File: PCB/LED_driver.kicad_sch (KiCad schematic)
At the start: 20 parts, among them J3 LED_GRBWA, J4 LED 5050, Q3 UMW30N06, Q4 UMW30N06, Q5 UMW30N06, U7 MCP1416, U8 MCP1416

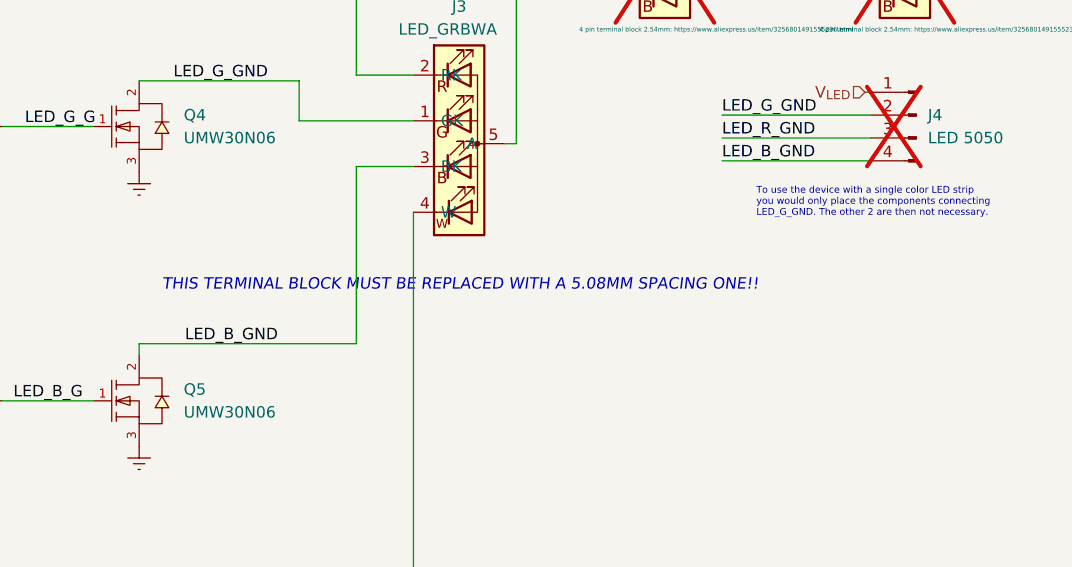
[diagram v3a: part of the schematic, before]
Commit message: design v1.0 - complete redesign
* redid schematic
* changed to screw terminal
* added W channel for RGBW strips
* did layout
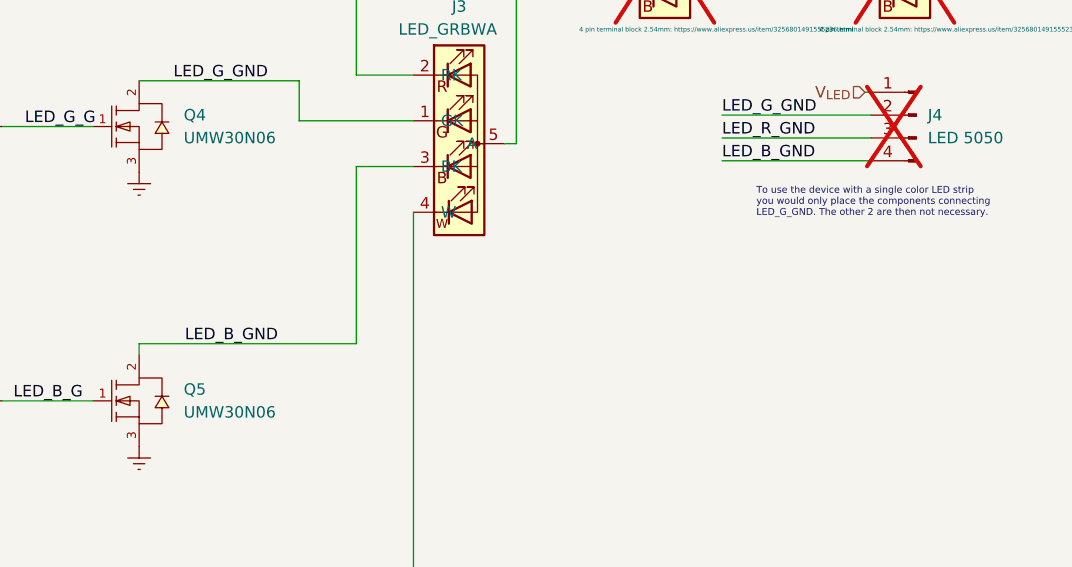
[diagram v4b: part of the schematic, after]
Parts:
- D2, J4: LCSC (none) -> -
- J3: LCSC (none) -> C5188445; Note (none) -> 5 pin 2.54 Pitch Terminal Block
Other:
- note removed: "THIS TERMINAL BLOCK MUST BE REPLACED WITH A 5.08MM SPACING ONE!!"
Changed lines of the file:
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@@
     (effects (font (size 1.27 1.27)) (justify left bottom))
-  )
-  (text "THIS TERMINAL BLOCK MUST BE REPLACED WITH A 5.08MM SPACING ONE!!"
-    (at 161.29 96.52 0)
-    (effects (font (size 1.27 1.27) italic) (justify left bottom))
   )
   (label "LED_R_GND" (at 223.52 79.375 0) (fields_autoplaced)
@@
         )
       )
-      (project "dumb-led-driver"
+      (project "iot_pwm_leddriver"
         (path "/b6358773-9a18-4eb2-bc1b-d38393a8df39/906d9b01-c5b2-4615-86e8-3c8294737d59"
           (reference "C4") (unit 1)
@@
         )
       )
-      (project "dumb-led-driver"
+      (project "iot_pwm_leddriver"
         (path "/b6358773-9a18-4eb2-bc1b-d38393a8df39/906d9b01-c5b2-4615-86e8-3c8294737d59"
           (reference "C3") (unit 1)
@@
         )
       )
-      (project "dumb-led-driver"
+      (project "iot_pwm_leddriver"
         (path "/b6358773-9a18-4eb2-bc1b-d38393a8df39/906d9b01-c5b2-4615-86e8-3c8294737d59"
           (reference "#PWR015") (unit 1)
@@
         )
       )
-      (project "dumb-led-driver"
+      (project "iot_pwm_leddriver"
         (path "/b6358773-9a18-4eb2-bc1b-d38393a8df39/906d9b01-c5b2-4615-86e8-3c8294737d59"
           (reference "#PWR016") (unit 1)
@@
         )
       )
-      (project "dumb-led-driver"
+      (project "iot_pwm_leddriver"
         (path "/b6358773-9a18-4eb2-bc1b-d38393a8df39/906d9b01-c5b2-4615-86e8-3c8294737d59"
           (reference "R10") (unit 1)
@@
       (effects (font (size 1.27 1.27)) hide)
     )
+    (property "LCSC" "-" (at 245.11 76.835 0)
+      (effects (font (size 1.27 1.27)) hide)
+    )
     (pin "1")
     (pin "2")
@@
         )
       )
-      (project "dumb-led-driver"
+      (project "iot_pwm_leddriver"
         (path "/b6358773-9a18-4eb2-bc1b-d38393a8df39/906d9b01-c5b2-4615-86e8-3c8294737d59"
           (reference "J4") (unit 1)
@@
         )
       )
-      (project "dumb-led-driver"
+      (project "iot_pwm_leddriver"
         (path "/b6358773-9a18-4eb2-bc1b-d38393a8df39/906d9b01-c5b2-4615-86e8-3c8294737d59"
           (reference "#PWR013") (unit 1)
@@
       (effects (font (size 1.27 1.27)) hide)
     )
+    (property "LCSC" "-" (at 217.17 58.42 0)
+      (effects (font (size 1.27 1.27)) hide)
+    )
     (pin "1")
     (pin "2")
@@
         )
       )
-      (project "dumb-led-driver"
+      (project "iot_pwm_leddriver"
         (path "/b6358773-9a18-4eb2-bc1b-d38393a8df39/906d9b01-c5b2-4615-86e8-3c8294737d59"
           (reference "D4") (unit 1)
@@
         )
       )
-      (project "dumb-led-driver"
+      (project "iot_pwm_leddriver"
         (path "/b6358773-9a18-4eb2-bc1b-d38393a8df39/906d9b01-c5b2-4615-86e8-3c8294737d59"
           (reference "R8") (unit 1)
@@
     )
     (property "LCSC" "C83775 " (at 113.665 44.45 0)
+      (effects (font (size 1.27 1.27)) hide)
+    )
+    (property "Description" "alternatively: https://www.lcsc.com/product-detail/Gate-Drive-ICs_JSMSEMI-MCP1416T-E-OT-JSM_C18195002.html" (at 113.665 44.45 0)
       (effects (font (size 1.27 1.27)) hide)
     )
@@
         )
       )
-      (project "dumb-led-driver"
+      (project "iot_pwm_leddriver"
         (path "/b6358773-9a18-4eb2-bc1b-d38393a8df39/906d9b01-c5b2-4615-86e8-3c8294737d59"
           (reference "U2") (unit 1)
@@
         )
       )
-      (project "dumb-led-driver"
+      (project "iot_pwm_leddriver"
         (path "/b6358773-9a18-4eb2-bc1b-d38393a8df39/906d9b01-c5b2-4615-86e8-3c8294737d59"
           (reference "C2") (unit 1)
@@
         )
       )
-      (project "dumb-led-driver"
+      (project "iot_pwm_leddriver"
         (path "/b6358773-9a18-4eb2-bc1b-d38393a8df39/906d9b01-c5b2-4615-86e8-3c8294737d59"
           (reference "#PWR026") (unit 1)
@@
         )
       )
-      (project "dumb-led-driver"
+      (project "iot_pwm_leddriver"
         (path "/b6358773-9a18-4eb2-bc1b-d38393a8df39/906d9b01-c5b2-4615-86e8-3c8294737d59"
           (reference "Q4") (unit 1)
@@
         )
       )
-      (project "dumb-led-driver"
+      (project "iot_pwm_leddriver"
         (path "/b6358773-9a18-4eb2-bc1b-d38393a8df39/906d9b01-c5b2-4615-86e8-3c8294737d59"
           (reference "R7") (unit 1)
@@
         )
       )
-      (project "dumb-led-driver"
+      (project "iot_pwm_leddriver"
         (path "/b6358773-9a18-4eb2-bc1b-d38393a8df39/906d9b01-c5b2-4615-86e8-3c8294737d59"
           (reference "R11") (unit 1)
@@
       (effects (font (size 1.27 1.27)) hide)
     )
+    (property "LCSC" "-" (at 243.84 58.42 0)
+      (effects (font (size 1.27 1.27)) hide)
+    )
     (pin "1")
     (pin "2")
@@
         )
       )
-      (project "dumb-led-driver"
+      (project "iot_pwm_leddriver"
         (path "/b6358773-9a18-4eb2-bc1b-d38393a8df39/906d9b01-c5b2-4615-86e8-3c8294737d59"
           (reference "D3") (unit 1)
@@
     )
     (property "LCSC" "C83775 " (at 115.57 140.97 0)
+      (effects (font (size 1.27 1.27)) hide)
+    )
+    (property "Description" "alternatively: https://www.lcsc.com/product-detail/Gate-Drive-ICs_JSMSEMI-MCP1416T-E-OT-JSM_C18195002.html" (at 115.57 140.97 0)
       (effects (font (size 1.27 1.27)) hide)
     )
@@
         )
       )
-      (project "dumb-led-driver"
+      (project "iot_pwm_leddriver"
         (path "/b6358773-9a18-4eb2-bc1b-d38393a8df39/906d9b01-c5b2-4615-86e8-3c8294737d59"
           (reference "U3") (unit 1)
@@
     )
     (property "LCSC" "C83775 " (at 114.935 108.585 0)
+      (effects (font (size 1.27 1.27)) hide)
+    )
+    (property "Description" "alternatively: https://www.lcsc.com/product-detail/Gate-Drive-ICs_JSMSEMI-MCP1416T-E-OT-JSM_C18195002.html" (at 114.935 108.585 0)
       (effects (font (size 1.27 1.27)) hide)
     )
@@
         )
       )
-      (project "dumb-led-driver"
+      (project "iot_pwm_leddriver"
         (path "/b6358773-9a18-4eb2-bc1b-d38393a8df39/906d9b01-c5b2-4615-86e8-3c8294737d59"
           (reference "U5") (unit 1)
@@
         )
       )
-      (project "dumb-led-driver"
+      (project "iot_pwm_leddriver"
         (path "/b6358773-9a18-4eb2-bc1b-d38393a8df39/906d9b01-c5b2-4615-86e8-3c8294737d59"
           (reference "#PWR020") (unit 1)
@@
         )
       )
-      (project "dumb-led-driver"
+      (project "iot_pwm_leddriver"
         (path "/b6358773-9a18-4eb2-bc1b-d38393a8df39/906d9b01-c5b2-4615-86e8-3c8294737d59"
           (reference "Q1") (unit 1)
@@
         )
       )
-      (project "dumb-led-driver"
+      (project "iot_pwm_leddriver"
         (path "/b6358773-9a18-4eb2-bc1b-d38393a8df39/906d9b01-c5b2-4615-86e8-3c8294737d59"
           (reference "#PWR012") (unit 1)
@@
     )
     (property "LCSC" "C83775 " (at 113.665 78.105 0)
+      (effects (font (size 1.27 1.27)) hide)
+    )
+    (property "Description" "alternatively: https://www.lcsc.com/product-detail/Gate-Drive-ICs_JSMSEMI-MCP1416T-E-OT-JSM_C18195002.html" (at 113.665 78.105 0)
       (effects (font (size 1.27 1.27)) hide)
     )
@@
         )
       )
-      (project "dumb-led-driver"
+      (project "iot_pwm_leddriver"
         (path "/b6358773-9a18-4eb2-bc1b-d38393a8df39/906d9b01-c5b2-4615-86e8-3c8294737d59"
           (reference "U4") (unit 1)
@@
         )
       )
-      (project "dumb-led-driver"
+      (project "iot_pwm_leddriver"
         (path "/b6358773-9a18-4eb2-bc1b-d38393a8df39/906d9b01-c5b2-4615-86e8-3c8294737d59"
           (reference "Q2") (unit 1)
@@
         )
       )
-      (project "dumb-led-driver"
+      (project "iot_pwm_leddriver"
         (path "/b6358773-9a18-4eb2-bc1b-d38393a8df39/906d9b01-c5b2-4615-86e8-3c8294737d59"
           (reference "#PWR027") (unit 1)
@@
         )
       )
-      (project "dumb-led-driver"
+      (project "iot_pwm_leddriver"
         (path "/b6358773-9a18-4eb2-bc1b-d38393a8df39/906d9b01-c5b2-4615-86e8-3c8294737d59"
           (reference "#PWR024") (unit 1)
@@
         )
       )
-      (project "dumb-led-driver"
+      (project "iot_pwm_leddriver"
         (path "/b6358773-9a18-4eb2-bc1b-d38393a8df39/906d9b01-c5b2-4615-86e8-3c8294737d59"
           (reference "Q3") (unit 1)
@@
       (effects (font (size 1.27 1.27)) hide)
     )
-    (property "Datasheet" "" (at 191.77 90.17 0)
-      (effects (font (size 1.27 1.27)) hide)
-    )
-    (property "Description" "FIX SELECTION OF TERMINAL BLOCK, MUST SOURCE ONE CORRECTLY!!!" (at 191.77 90.17 0)
+    (property "Datasheet" "https://www.lcsc.com/product-detail/Screw-terminal_MAX-MX128-2-54-05P-GN01-Cu-Y-A_C5188445.html" (at 191.77 90.17 0)
+      (effects (font (size 1.27 1.27)) hide)
+    )
+    (property "Description" "MX128-2.54-05P-GN01-Cu-Y-A" (at 191.77 90.17 0)
+      (effects (font (size 1.27 1.27)) hide)
+    )
+    (property "LCSC" "C5188445" (at 191.77 90.17 0)
+      (effects (font (size 1.27 1.27)) hide)
+    )
+    (property "Note" "5 pin 2.54 Pitch Terminal Block" (at 191.77 90.17 0)
       (effects (font (size 1.27 1.27)) hide)
     )
@@
     (pin "5")
     (instances
-      (project "dumb-led-driver"
+      (project "iot_pwm_leddriver"
         (path "/b6358773-9a18-4eb2-bc1b-d38393a8df39/906d9b01-c5b2-4615-86e8-3c8294737d59"
           (reference "J3") (unit 1)
@@
         )
       )
-      (project "dumb-led-driver"
+      (project "iot_pwm_leddriver"
         (path "/b6358773-9a18-4eb2-bc1b-d38393a8df39/906d9b01-c5b2-4615-86e8-3c8294737d59"
           (reference "C6") (unit 1)

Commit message: schematic and layout cleanup
* plus BOM finalization
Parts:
- removed D2: LED_RBGA, TerminalBlock_Phoenix:TerminalBlock_Phoenix_MPT-0,5-4-2.54_1x04_P2.54mm_Horizontal, symbol Device:LED_RBGA
- removed J4: LED 5050, Connector_PinHeader_2.54mm:PinHeader_1x04_P2.54mm_Vertical, symbol Connector:Conn_01x04_Male
- D2: Note 4 pin terminal block 2.54mm: https://www.aliexpress.us/item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 -> solder wire connector
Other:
- note added: "5m 5050 RGB LED Strip expected to draw max ~6A Math: P = VI, I_{total} = (Num_{LEDs}/m) * length(m) (.24W * 60 LEDs/m * 5m)/12V = 6A (But, will be lower irl due to R of copper in LED strip) Fuse rating = (Current / .75) = (6/.75) = 8A"
- note added: "This component is a stand-in for the LED strip, and corresponds to the screw terminal block on the board"
- note removed: "5m 5050 LED Strip expected to draw max ~6A Math: P = VI, I_{total} = (Num_{LEDs}/m) * length(m) (.24W * 60 LEDs/m * 5m)/12V = 6A (But, will be lower irl due to R of copper in LED strip) Fuse rating = (Current / .75) = (6/.75) = 8A"
- note removed: "This component is a stand-in for the LED strip, and corresponds to the strain relief connector on the board"
- note removed: "To use the device with a single color LED strip you would only place the components connecting LED_G_GND. The other 2 are then not necessary."
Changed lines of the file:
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@@
   (junction (at 113.665 66.675) (diameter 0) (color 0 0 0 0)
   )
-  (junction (at 238.76 58.42) (diameter 0) (color 0 0 0 0)
-  )
   (junction (at 212.09 53.34) (diameter 0) (color 0 0 0 0)
   )
   (junction (at 114.935 116.205) (diameter 0) (color 0 0 0 0)
   )
-  (junction (at 238.76 53.34) (diameter 0) (color 0 0 0 0)
-  )
   (junction (at 113.665 52.07) (diameter 0) (color 0 0 0 0)
   )
@@
     (stroke (width 0) (type default))
   )
-  (wire (pts (xy 238.76 58.42) (xy 238.76 63.5))
-    (stroke (width 0) (type default))
-  )
-  (wire (pts (xy 223.52 79.375) (xy 240.03 79.375))
-    (stroke (width 0) (type default))
-  )
   (wire (pts (xy 114.935 98.425) (xy 127.635 98.425))
     (stroke (width 0) (type default))
@@
     (stroke (width 0) (type default))
   )
-  (wire (pts (xy 238.76 46.99) (xy 238.76 53.34))
-    (stroke (width 0) (type default))
-  )
   (wire (pts (xy 159.385 134.62) (xy 189.23 134.62))
     (stroke (width 0) (type default))
   )
-  (wire (pts (xy 239.395 74.295) (xy 240.03 74.295))
-    (stroke (width 0) (type default))
-  )
   (wire (pts (xy 126.365 34.29) (xy 126.365 33.02))
     (stroke (width 0) (type default))
   )
-  (wire (pts (xy 223.52 81.915) (xy 240.03 81.915))
-    (stroke (width 0) (type default))
-  )
   (wire (pts (xy 212.09 48.26) (xy 212.09 53.34))
     (stroke (width 0) (type default))
   )
-  (wire (pts (xy 223.52 76.835) (xy 240.03 76.835))
-    (stroke (width 0) (type default))
-  )
   (wire (pts (xy 126.365 52.07) (xy 113.665 52.07))
     (stroke (width 0) (type default))
@@
     (stroke (width 0) (type default))
   )
-  (wire (pts (xy 248.92 46.99) (xy 238.76 46.99))
-    (stroke (width 0) (type default))
-  )
   (wire (pts (xy 128.27 130.81) (xy 128.27 132.08))
     (stroke (width 0) (type default))
@@
     (stroke (width 0) (type default))
   )
-  (wire (pts (xy 238.76 53.34) (xy 238.76 58.42))
-    (stroke (width 0) (type default))
-  )
   (wire (pts (xy 127.635 98.425) (xy 127.635 99.695))
     (stroke (width 0) (type default))
@@
     (stroke (width 0) (type default))
   )
-  (wire (pts (xy 248.92 58.42) (xy 248.92 46.99))
-    (stroke (width 0) (type default))
-  )
   (wire (pts (xy 212.09 53.34) (xy 212.09 58.42))
     (stroke (width 0) (type default))
@@
     (stroke (width 0) (type default))
   )
-  (text "To use the device with a single color LED strip\nyou would only place the components connecting \nLED_G_GND. The other 2 are then not necessary. "
-    (at 227.33 88.265 0)
-    (effects (font (size 0.762 0.762)) (justify left bottom))
-  )
-  (text "This component is a stand-in \nfor the LED strip, and \ncorresponds to the strain \nrelief connector on the board"
-    (at 213.36 40.64 0)
+  (text "This component is a stand-in \nfor the LED strip, and \ncorresponds to the screw \nterminal block on the board"
+    (at 192.405 101.6 0)
     (effects (font (size 1.27 1.27)) (justify left bottom))
   )
@@
     (effects (font (size 1.27 1.27)) (justify left bottom))
   )
-  (text "5m 5050 LED Strip expected to draw max ~6A\nMath: \n	P = VI, I_{total} = (Num_{LEDs}/m) * length(m)\n	(.24W * 60 LEDs/m * 5m)/12V = 6A\n	(But, will be lower irl due to R of copper in LED strip)\n	Fuse rating = (Current / .75) = (6/.75) = 8A"
+  (text "5m 5050 RGB LED Strip expected to draw max ~6A\nMath: \n	P = VI, I_{total} = (Num_{LEDs}/m) * length(m)\n	(.24W * 60 LEDs/m * 5m)/12V = 6A\n	(But, will be lower irl due to R of copper in LED strip)\n	Fuse rating = (Current / .75) = (6/.75) = 8A"
     (at 25.781 98.806 0)
     (effects (font (size 1.27 1.27)) (justify left bottom))
   )
-  (label "LED_R_GND" (at 223.52 79.375 0) (fields_autoplaced)
-    (effects (font (size 1.27 1.27)) (justify left bottom))
-  )
   (label "LED_R_GND" (at 171.45 39.37 0) (fields_autoplaced)
     (effects (font (size 1.27 1.27)) (justify left bottom))
@@
     (effects (font (size 1.27 1.27)) (justify left bottom))
   )
-  (label "LED_G_GND" (at 223.52 76.835 0) (fields_autoplaced)
-    (effects (font (size 1.27 1.27)) (justify left bottom))
-  )
   (label "LED_G_GND" (at 162.56 73.025 0) (fields_autoplaced)
     (effects (font (size 1.27 1.27)) (justify left bottom))
@@
     (effects (font (size 1.27 1.27)) (justify left bottom))
   )
-  (label "LED_B_GND" (at 223.52 81.915 0) (fields_autoplaced)
-    (effects (font (size 1.27 1.27)) (justify left bottom))
-  )
   (label "LED_B_GND" (at 163.83 102.235 0) (fields_autoplaced)
     (effects (font (size 1.27 1.27)) (justify left bottom))
@@
   )
   (hierarchical_label "V_{LED}" (shape input) (at 112.395 66.675 180) (fields_autoplaced)
-    (effects (font (size 1.27 1.27)) (justify right))
-  )
-  (hierarchical_label "V_{LED}" (shape input) (at 239.395 74.295 180) (fields_autoplaced)
     (effects (font (size 1.27 1.27)) (justify right))
   )
@@
     )
   )
-  (symbol (lib_id "Connector:Conn_01x04_Male") (at 245.11 76.835 0) (mirror y) (unit 1)
-    (in_bom no) (on_board no) (dnp yes) (fields_autoplaced)
-    (property "Reference" "J4" (at 246.38 76.8349 0)
-      (effects (font (size 1.27 1.27)) (justify right))
-    )
-    (property "Value" "LED 5050" (at 246.38 79.3749 0)
-      (effects (font (size 1.27 1.27)) (justify right))
-    )
-    (property "Footprint" "Connector_PinHeader_2.54mm:PinHeader_1x04_P2.54mm_Vertical" (at 245.11 76.835 0)
-      (effects (font (size 1.27 1.27)) hide)
-    )
-    (property "Datasheet" "~" (at 245.11 76.835 0)
-      (effects (font (size 1.27 1.27)) hide)
-    )
-    (property "LCSC" "-" (at 245.11 76.835 0)
-      (effects (font (size 1.27 1.27)) hide)
-    )
-    (pin "1")
-    (pin "2")
-    (pin "3")
-    (pin "4")
-    (instances
-      (project "iot_led_strip_pcb"
-        (path "/745f5767-ebad-4719-b66e-073bc90db4bc/af18acc8-a8c3-4e1e-8a57-49b565af3262"
-          (reference "J4") (unit 1)
-        )
-      )
-      (project "iot_pwm_leddriver"
-        (path "/b6358773-9a18-4eb2-bc1b-d38393a8df39/906d9b01-c5b2-4615-86e8-3c8294737d59"
-          (reference "J4") (unit 1)
-        )
-      )
-      (project "LED_driver"
-        (path "/dc96e041-5ba7-4eeb-baa0-ca65355a480c"
-          (reference "J4") (unit 1)
-        )
-      )
-    )
-  )
   (symbol (lib_id "power:Earth") (at 114.935 116.205 0) (unit 1)
     (in_bom yes) (on_board yes) (dnp no) (fields_autoplaced)
@@
   )
   (symbol (lib_id "Device:LED_RBGA") (at 217.17 58.42 0) (unit 1)
-    (in_bom no) (on_board no) (dnp yes) (fields_autoplaced)
+    (in_bom no) (on_board no) (dnp yes)
     (property "Reference" "D2" (at 217.17 45.085 0)
       (effects (font (size 1.27 1.27)))
@@
       (effects (font (size 1.27 1.27)) hide)
     )
-    (property "Note" "4 pin terminal block 2.54mm: https://www.aliexpress.us/item/3256801491555236.html" (at 222.885 67.31 0)
+    (property "Note" "solder wire connector" (at 217.17 67.31 0)
       (effects (font (size 0.508 0.508)))
     )
@@
         )
       )
-    )
-  )
-  (symbol (lib_id "Device:LED_RBGA") (at 243.84 58.42 0) (unit 1)
-    (in_bom no) (on_board no) (dnp yes) (fields_autoplaced)
-    (property "Reference" "D2" (at 243.84 45.085 0)
-      (effects (font (size 1.27 1.27)))
-    )
-    (property "Value" "LED_RBGA" (at 243.84 47.625 0)
-      (effects (font (size 1.27 1.27)))
-    )
-    (property "Footprint" "TerminalBlock_Phoenix:TerminalBlock_Phoenix_MPT-0,5-4-2.54_1x04_P2.54mm_Horizontal" (at 243.84 59.69 0)
-      (effects (font (size 1.27 1.27)) hide)
-    )
-    (property "Datasheet" "~" (at 243.84 59.69 0)
-      (effects (font (size 1.27 1.27)) hide)
-    )
-    (property "Note" "4 pin terminal block 2.54mm: https://www.aliexpress.us/item/3256801491555236.html" (at 249.555 67.31 0)
-      (effects (font (size 0.508 0.508)))
-    )
-    (property "Sim.Enable" "0" (at 243.84 58.42 0)
-      (effects (font (size 1.27 1.27)) hide)
-    )
-    (property "LCSC" "-" (at 243.84 58.42 0)
-      (effects (font (size 1.27 1.27)) hide)
-    )
-    (pin "1")
-    (pin "2")
-    (pin "3")
-    (pin "4")
-    (instances
-      (project "iot_led_strip_pcb"
-        (path "/745f5767-ebad-4719-b66e-073bc90db4bc/af18acc8-a8c3-4e1e-8a57-49b565af3262"
-          (reference "D2") (unit 1)
-        )
-      )
-      (project "iot_pwm_leddriver"
-        (path "/b6358773-9a18-4eb2-bc1b-d38393a8df39/906d9b01-c5b2-4615-86e8-3c8294737d59"
-          (reference "D3") (unit 1)
-        )
-      )
-      (project "LED_driver"
-        (path "/dc96e041-5ba7-4eeb-baa0-ca65355a480c"
-          (reference "D2") (unit 1)
-        )
-      )
